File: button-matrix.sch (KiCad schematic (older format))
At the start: 74 parts, among them SW301 TL1105T, SW302 TL1105T, SW303 TL1105T, SW304 TL1105T, SW305 TL1105T, SW309 TL1105T, SW310 TL1105T, SW311 TL1105T, SW312 TL1105T, SW313 TL1105T, SW314 TL1105T, SW315 TL1105T, SW316 TL1105T, SW317 TL1105T, SW318 TL1105T, SW319 TL1105T, SW320 TL1105T, SW321 TL1105T, SW322 TL1105T, SW323 TL1105T, SW324 TL1105T, SW325 TL1105T, SW326 TL1105T, SW327 TL1105T, SW328 TL1105T, SW329 TL1105T, SW330 TL1105T, SW331 TL1105T, SW332 TL1105T, SW333 TL1105T, SW334 TL1105T, SW335 TL1105T, SW336 TL1105T, SW337 TL1105T, SW338 TL1105T, SW339 TL1105T, SW340 TL1105T

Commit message: renumbered pcb
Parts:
- renumbered D304 to D10, D305 to D11, D311 to D12, D312 to D13, D317 to D14, D318 to D15, D319 to D16, D320 to D17, D321 to D18, D322 to D19, D323 to D20, D324 to D21, D313 to D22, D314 to D23, D325 to D24, D326 to D25, D327 to D26, D328 to D27, D329 to D28, D330 to D29, D331 to D30, D332 to D31, D316 to D32, D333 to D33, D315 to D34, D334 to D35, D335 to D36, D336 to D37, D337 to D38, D338 to D39, D339 to D40, D340 to D41, D309 to D5, D310 to D6, D301 to D7, D302 to D8, D303 to D9, SW309 to SW1, SW312 to SW10, SW317 to SW11, SW318 to SW12, SW319 to SW13, SW320 to SW14, SW321 to SW15, SW322 to SW16, SW323 to SW17, SW324 to SW18, SW310 to SW2, SW313 to SW20, SW314 to SW21, SW325 to SW22, SW326 to SW23, SW327 to SW24, SW328 to SW25, SW329 to SW26, SW330 to SW27, SW331 to SW28, SW332 to SW29, SW301 to SW3, SW315 to SW30, SW316 to SW31, SW333 to SW32, SW334 to SW33, SW335 to SW34, SW336 to SW35, SW337 to SW36, SW338 to SW37, SW339 to SW38, SW340 to SW39, SW302 to SW4, SW303 to SW5, SW304 to SW6, SW305 to SW7, SW311 to SW9

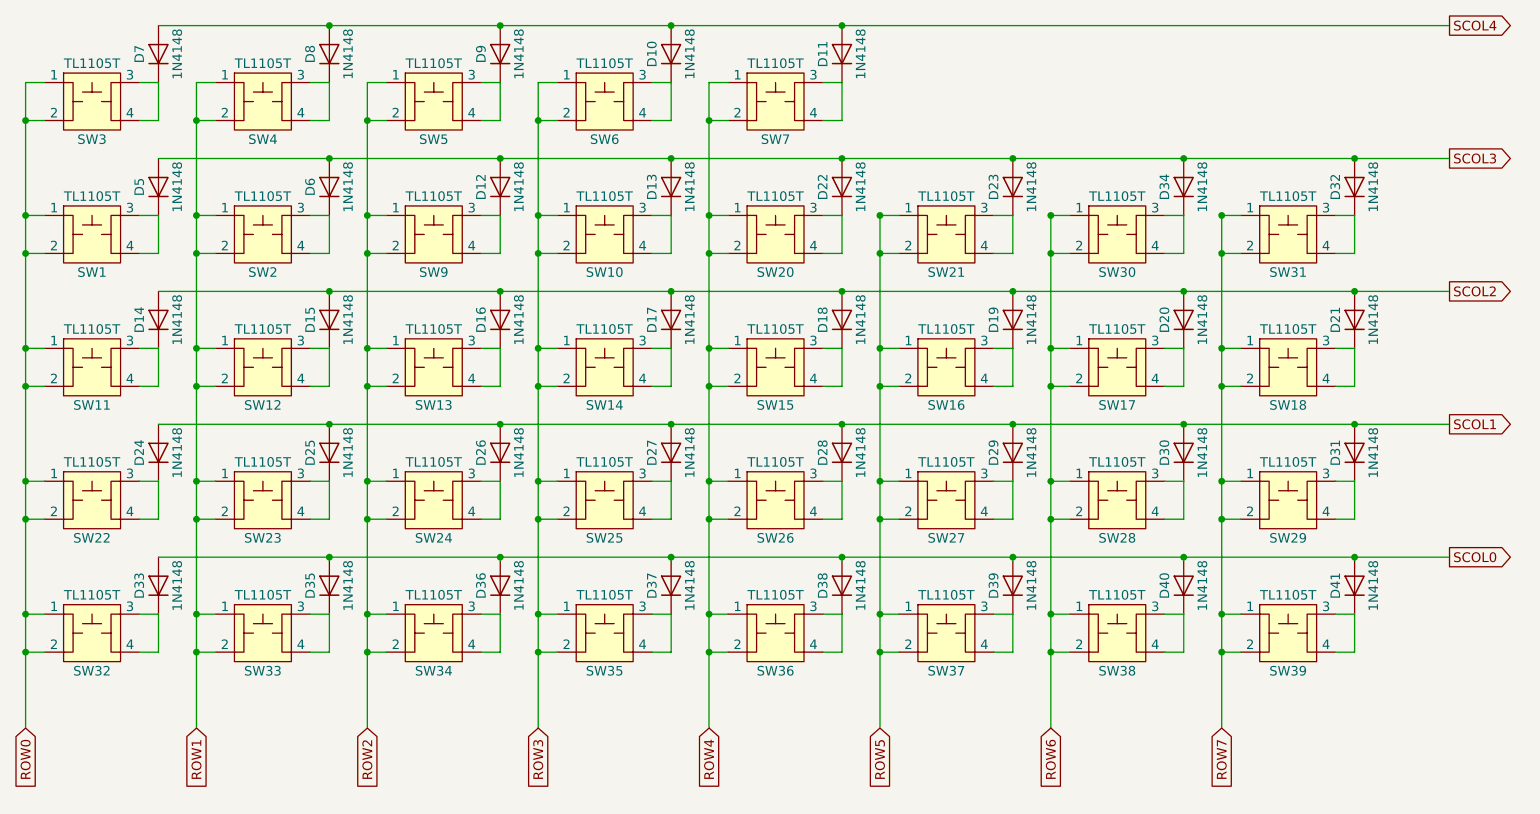
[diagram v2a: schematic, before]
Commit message: corrected some part values
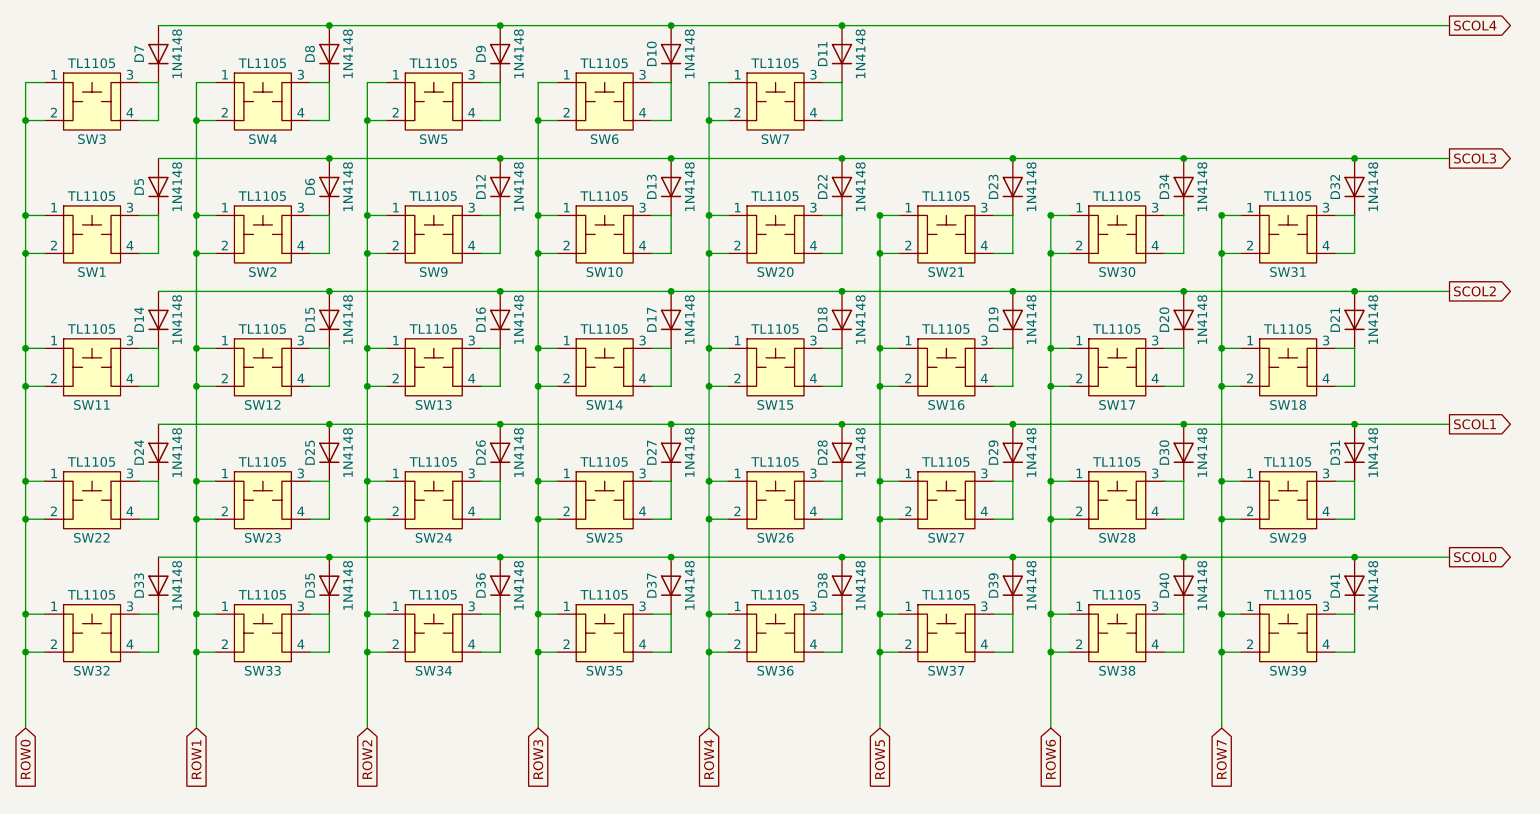
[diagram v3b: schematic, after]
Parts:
- SW1, SW10, SW11, SW12, SW13, SW14, SW15, SW16, SW17, SW18, SW2, SW20, SW21, SW22, SW23, SW24, SW25, SW26, SW27, SW28, SW29, SW3, SW30, SW31, SW32, SW33, SW34, SW35, SW36, SW37, SW38, SW39, SW4, SW5, SW6, SW7, SW9: value TL1105T -> TL1105; MFP TL1105TF160Q -> TL1105SPF160Q
